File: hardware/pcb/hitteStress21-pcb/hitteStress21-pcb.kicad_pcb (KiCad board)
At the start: 2 copper layers, 90 x 119 mm, 17 parts, among them J1 Conn_01x02_Female, J2 Conn_01x05, J3 Conn_01x03, U1 HTCC-AB01, U2 GPS

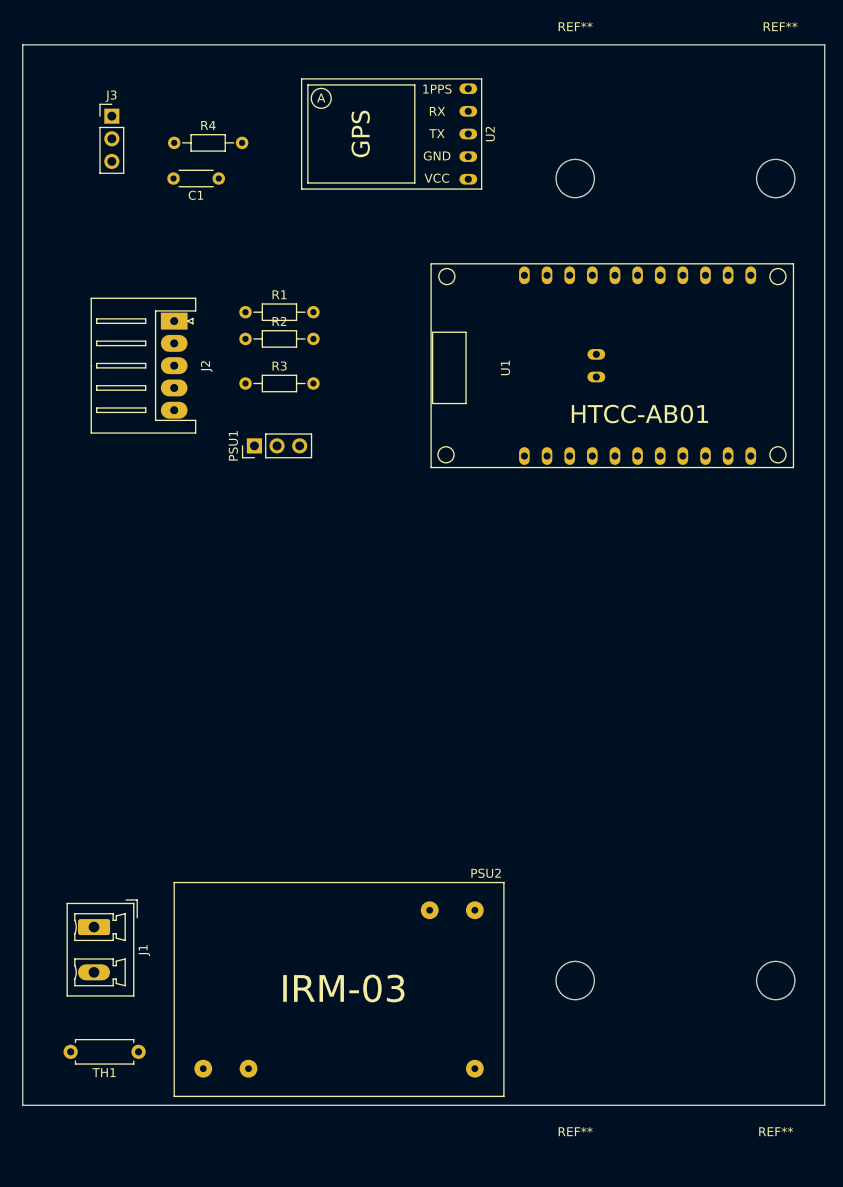
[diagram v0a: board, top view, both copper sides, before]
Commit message: Updates on footprints
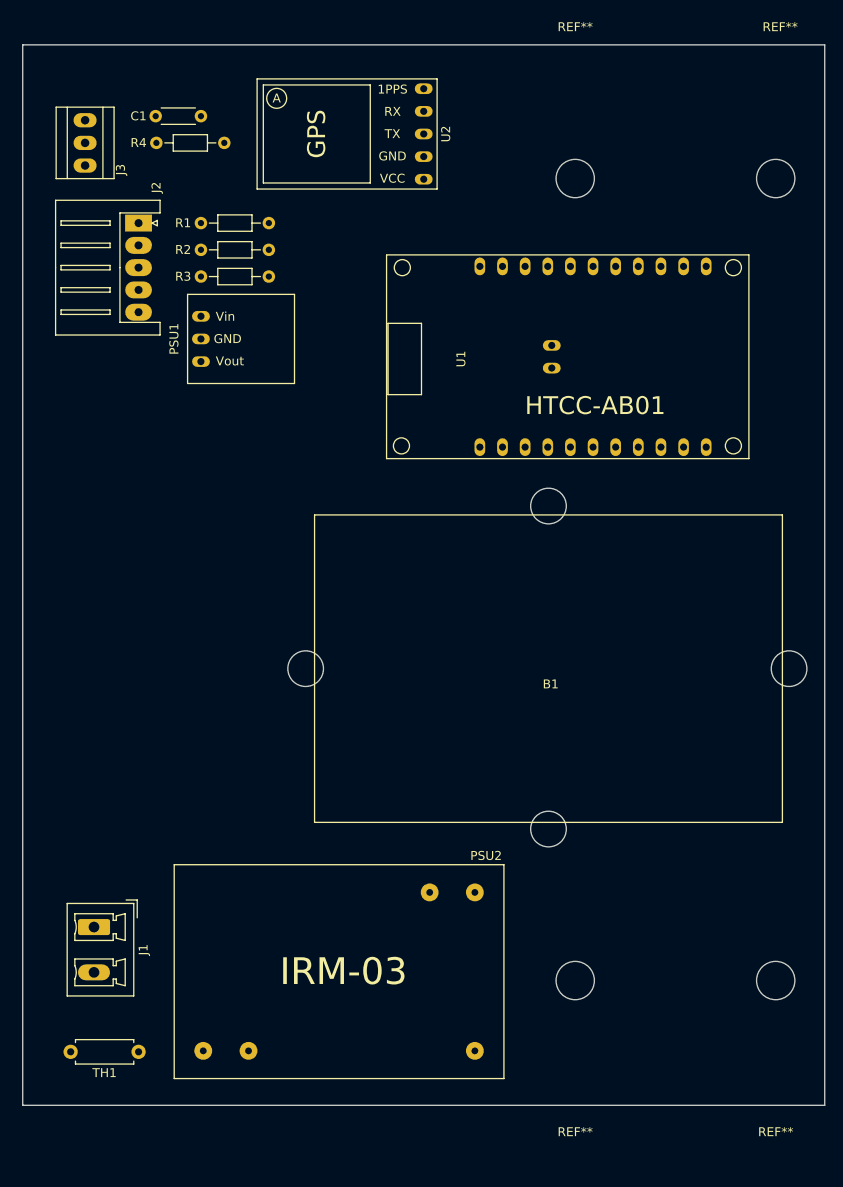
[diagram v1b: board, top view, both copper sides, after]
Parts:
- added B1: LiPo_3V7, hitteStress21-pcb:LiPo_3V7_2000mAh_JST-PH, F.Cu at (220.0, 107.0)
- J3: footprint Connector_PinHeader_2.54mm:PinHeader_1x03_P2.54mm_Vertical -> hitteStress21-pcb:Wurth_2109_p2.54
- PSU1: footprint Connector_PinHeader_2.54mm:PinHeader_1x03_P2.54mm_Vertical -> hitteStress21-pcb:MINIDCBOOST5V
- moved PSU1 13.4 mm to (181.0, 70.0)
- moved R3 13.0 mm to (181.0, 63.0)
- moved J2 11.7 mm to (174.0, 57.0)
- moved R1 11.2 mm to (181.0, 57.0)
- moved R2 11.2 mm to (181.0, 60.0)
- moved C1 7.28 mm to (181.0, 45.0)
- moved U1 5.10 mm to (225.0, 72.0)
- moved U2 5.00 mm to (206.0, 47.0)
- moved J3 4.24 mm to (168.0, 48.0), turned to 90 degrees
- moved PSU2 2.00 mm to (215.0, 129.0)
- moved R4 2.00 mm to (176.0, 48.0)
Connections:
- R1 pad 2: /SDS011_RX -> /SDS011_TX
- R2 pad 2: /SDS011_TX -> /SDS011_RX

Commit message: PCB design updates
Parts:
- added G***: LOGO_LogoRFSee_37x8mm, hitteStress21-pcb:LOGO_LogoRFSee_37x8mm, F.Cu at (219.0, 108.0)
- added G***: LOGO, hitteStress21-pcb:TTN_Apld_Logo_17x17mm_silk, F.Cu at (177.0, 97.0)
- added J4: Conn_01x02, hitteStress21-pcb:Wurth_2109_P2.54_2x1, F.Cu at (167.5, 85.5)
- moved J1 11.5 mm to (169.0, 124.5)
- moved J2 7.52 mm to (173.5, 64.5)
- moved PSU1 7.52 mm to (180.5, 77.5)
- moved R1 7.52 mm to (180.5, 64.5)
- moved R2 7.52 mm to (180.5, 67.5)
- moved R3 7.52 mm to (180.5, 70.5)
- moved U2 5.15 mm to (208.5, 51.5)
- moved C1 4.53 mm to (180.5, 49.5)
- moved J3 4.53 mm to (167.5, 52.5)
- moved R4 4.53 mm to (175.5, 52.5)
- moved PSU2 3.00 mm to (215.0, 126.0)
- moved TH1 3.00 mm to (174.0, 147.0)
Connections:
- R1 pad 2: /SDS011_TX -> /SDS011_TXD
- R2 pad 2: /SDS011_RX -> /SDS011_RXD
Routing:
- net GND: track 0.00 -> 161.1 mm, vias 0 -> 64
- net /3V3: track 0.00 -> 100.4 mm
- net /5V: track 0.00 -> 100.0 mm
- net /PV: track 0.00 -> 76.5 mm
- net /AM2305_DATA: track 0.00 -> 55.0 mm
- net /3V3_EXT: track 0.00 -> 42.4 mm
- net /SDS011_TXD: track 0.00 -> 42.3 mm
- net /GPS_RXD: track 0.00 -> 40.2 mm
- net /GPS_TXD: track 0.00 -> 37.9 mm
- net Net-(J1-Pad1): track 0.00 -> 32.8 mm
- net /SDS011_RXD: track 0.00 -> 32.6 mm
- net Net-(J1-Pad2): track 0.00 -> 18.5 mm
- net /5V_EXT: track 0.00 -> 14.7 mm
- net Net-(J2-Pad4): track 0.00 -> 7.62 mm
- net Net-(PSU2-Pad1): track 0.00 -> 7.31 mm
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- added copper zone on B.Cu, net GND
- added copper zone on F.Cu, net GND
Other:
- board size 90 x 119 mm -> 90 x 109.9 mm
- board text added: "+"
- board text added: "-"
- board text added: "20210117"
- board text added: "3V3"
- board text added: "AC 220V"
- board text added: "AM2305"
- board text added: "DAT"
- board text added: "GND"
- board text added: "Hittestress sensor V2"
- board text added: "PV"
- board text added: "SDS011"
- board text added: "Stichting IoT Apeldoorn e/o www.iot-apeldoorn.ml"

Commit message: Modified HTCC-AB01 footprint and updated PCB accordingly
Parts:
- moved U1 8.06 mm to (217.0, 71.0)
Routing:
- net GND: track 161.1 -> 65.7 mm, vias 64 -> 62
- net /PV: track 76.5 -> 43.1 mm
- net /GPS_TXD: track 37.9 -> 61.3 mm
- net /3V3: track 100.4 -> 77.2 mm
- net /GPS_RXD: track 40.2 -> 61.9 mm
- net /3V3_EXT: track 42.4 -> 59.5 mm
- net /5V: track 100.0 -> 117.0 mm
- net /AM2305_DATA: track 55.0 -> 68.4 mm
- net /SDS011_RXD: track 32.6 -> 40.4 mm
- net /SDS011_TXD: track 42.3 -> 36.7 mm
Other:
- board text added: "20210216"
- board text removed: "20210117"

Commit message: UPdate PCD, added support holes for antenna supports
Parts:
- moved U2 4.00 mm to (212.5, 51.5)
- moved G*** 3.50 mm to (173.5, 97.0)
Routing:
- net /GPS_TXD: track 61.3 -> 57.3 mm
- net /GPS_RXD: track 61.9 -> 57.9 mm
- net /3V3_EXT: track 59.5 -> 55.5 mm
- net /AM2305_DATA: track 68.4 -> 71.3 mm
- net GND: vias 62 -> 61
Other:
- outline, holes or cut-outs redrawn
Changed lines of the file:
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@@
   (general
     (thickness 1.6)
-    (drawings 16)
-    (tracks 160)
+    (drawings 22)
+    (tracks 158)
     (zones 0)
     (modules 21)
@@
   )
   (setup
-    (last_trace_width 1)
+    (last_trace_width 0.25)
     (user_trace_width 0.5)
     (user_trace_width 0.75)
@@
   )
   (module hitteStress21-pcb:GPS (layer F.Cu)
-    (at 208.5 51.5)
+    (at 212.5 51.5)
     (fp_text reference U2 (at 2.75 5.5 180) (layer F.SilkS)
       (effects (font (size 1 1) (thickness 0.15)))
@@
   )
   (module hitteStress21-pcb:TTN_Apld_Logo_17x17mm_silk (layer F.Cu)
-    (at 177 97)
+    (at 173.5 97)
     (fp_text reference G*** (at 0 0) (layer F.SilkS) hide
       (effects (font (size 1.524 1.524) (thickness 0.3)))
@@
       (net 13 "Net-(U1-Pad22)"))
   )
-  (gr_text "Hittestress\nsensor V2" (at 177 110.5) (layer F.SilkS)
+  (gr_circle (center 185 110) (end 187.25 110) (layer Edge.Cuts) (width 0.1))
+  (gr_circle (center 185 102.38) (end 186.75 102.38) (layer Edge.Cuts) (width 0.1))
+  (gr_circle (center 243.5 73.5) (end 245.75 73.5) (layer Edge.Cuts) (width 0.1))
+  (gr_circle (center 243.5 65.88) (end 245.25 65.88) (layer Edge.Cuts) (width 0.1))
+  (gr_circle (center 188.5 49.38) (end 190.25 49.38) (layer Edge.Cuts) (width 0.1))
+  (gr_circle (center 188.5 57) (end 190.75 57) (layer Edge.Cuts) (width 0.1))
+  (gr_text "Hittestress\nsensor V2" (at 173.5 110.5) (layer F.SilkS)
     (effects (font (size 2 2) (thickness 0.5)))
   )
-  (gr_text "Stichting IoT Apeldoorn e/o\nwww.iot-apeldoorn.ml" (at 177 117.5) (layer F.SilkS)
+  (gr_text "Stichting IoT Apeldoorn e/o\nwww.iot-apeldoorn.ml" (at 173.5 117.5) (layer F.SilkS)
     (effects (font (size 1 1) (thickness 0.25)))
   )
@@
   (via (at 165 110) (size 0.8) (drill 0.4) (layers F.Cu B.Cu) (net 2))
   (via (at 175 110) (size 0.8) (drill 0.4) (layers F.Cu B.Cu) (net 2))
-  (via (at 185 110) (size 0.8) (drill 0.4) (layers F.Cu B.Cu) (net 2))
   (via (at 205 110) (size 0.8) (drill 0.4) (layers F.Cu B.Cu) (net 2))
   (via (at 205 120) (size 0.8) (drill 0.4) (layers F.Cu B.Cu) (net 2))
@@
   (via (at 205 100) (size 0.8) (drill 0.4) (layers F.Cu B.Cu) (net 2))
   (via (at 195 100) (size 0.8) (drill 0.4) (layers F.Cu B.Cu) (net 2))
-  (via (at 185 100) (size 0.8) (drill 0.4) (layers F.Cu B.Cu) (net 2))
   (via (at 175 100) (size 0.8) (drill 0.4) (layers F.Cu B.Cu) (net 2))
   (via (at 165 100) (size 0.8) (drill 0.4) (layers F.Cu B.Cu) (net 2))
@@
   (via (at 194.5 49.5) (size 0.8) (drill 0.4) (layers F.Cu B.Cu) (net 2))
   (via (at 204.5 49.5) (size 0.8) (drill 0.4) (layers F.Cu B.Cu) (net 2))
-  (via (at 215 50) (size 0.8) (drill 0.4) (layers F.Cu B.Cu) (net 2))
   (via (at 235 50) (size 0.8) (drill 0.4) (layers F.Cu B.Cu) (net 2))
+  (via (at 235 80) (size 0.8) (drill 0.4) (layers F.Cu B.Cu) (net 2))
+  (via (at 235 60) (size 0.8) (drill 0.4) (layers F.Cu B.Cu) (net 2))
   (segment (start 186.34 139.84) (end 186.34 146.89) (width 1.5) (layer F.Cu) (net 3))
   (segment (start 169 124.5) (end 174.5 124.5) (width 1.5) (layer F.Cu) (net 3))
@@
   (segment (start 176.5 72) (end 178 70.5) (width 0.5) (layer B.Cu) (net 7))
   (segment (start 167.5 52.5) (end 175.5 52.5) (width 0.5) (layer F.Cu) (net 9))
+  (segment (start 226.5 58.5) (end 227.16 59.16) (width 0.5) (layer F.Cu) (net 9))
   (segment (start 227.16 59.16) (end 227.16 60.86) (width 0.5) (layer F.Cu) (net 9))
-  (segment (start 226.5 58.5) (end 227.16 59.16) (width 0.5) (layer F.Cu) (net 9))
+  (segment (start 178 50) (end 178 49) (width 0.5) (layer F.Cu) (net 9))
+  (segment (start 182.5 44.5) (end 194.035082 44.5) (width 0.5) (layer F.Cu) (net 9))
+  (segment (start 175.5 52.5) (end 178 50) (width 0.5) (layer F.Cu) (net 9))
+  (segment (start 178 49) (end 182.5 44.5) (width 0.5) (layer F.Cu) (net 9))
   (segment (start 208.035082 58.5) (end 226.5 58.5) (width 0.5) (layer F.Cu) (net 9))
-  (segment (start 178 50) (end 178 49) (width 0.5) (layer F.Cu) (net 9))
-  (segment (start 175.5 52.5) (end 178 50) (width 0.5) (layer F.Cu) (net 9))
-  (segment (start 178 49) (end 179 48) (width 0.5) (layer F.Cu) (net 9))
-  (segment (start 179 48) (end 197.535082 48) (width 0.5) (layer F.Cu) (net 9))
-  (segment (start 197.535082 48) (end 208.035082 58.5) (width 0.5) (layer F.Cu) (net 9))
+  (segment (start 194.035082 44.5) (end 208.035082 58.5) (width 0.5) (layer F.Cu) (net 9))
   (segment (start 188.12 75.88) (end 188.12 70.5) (width 1) (layer F.Cu) (net 10))
   (segment (start 180.5 80.04) (end 183.96 80.04) (width 1) (layer F.Cu) (net 10))
@@
   (segment (start 226.6 45.3) (end 233.4 52.1) (width 0.5) (layer F.Cu) (net 17))
   (segment (start 219.9 45.3) (end 226.6 45.3) (width 0.5) (layer F.Cu) (net 17))
-  (segment (start 208.5 48.96) (end 216.24 48.96) (width 0.5) (layer F.Cu) (net 17))
   (segment (start 233.4 52.1) (end 233.4 69.8) (width 0.5) (layer F.Cu) (net 17))
+  (segment (start 216.24 48.96) (end 212.5 48.96) (width 0.5) (layer F.Cu) (net 17))
   (segment (start 188.12 64.5) (end 220.5 64.5) (width 0.5) (layer F.Cu) (net 18))
   (segment (start 222.08 62.92) (end 222.08 60.86) (width 0.5) (layer F.Cu) (net 18))
@@
   (segment (start 232.4 69.32) (end 222.08 79.64) (width 0.5) (layer F.Cu) (net 19))
   (segment (start 215.1 51.5) (end 220.2 46.4) (width 0.5) (layer F.Cu) (net 19))
-  (segment (start 208.5 51.5) (end 215.1 51.5) (width 0.5) (layer F.Cu) (net 19))
   (segment (start 226.1 46.4) (end 232.4 52.7) (width 0.5) (layer F.Cu) (net 19))
   (segment (start 220.2 46.4) (end 226.1 46.4) (width 0.5) (layer F.Cu) (net 19))
   (segment (start 232.4 52.7) (end 232.4 69.32) (width 0.5) (layer F.Cu) (net 19))
-  (segment (start 216.1 75) (end 211.92 79.18) (width 0.5) (layer F.Cu) (net 26))
-  (segment (start 231.4 58.9) (end 231.4 68.8) (width 0.5) (layer F.Cu) (net 26))
-  (segment (start 211.92 79.18) (end 211.92 81.14) (width 0.5) (layer F.Cu) (net 26))
-  (segment (start 231.4 68.8) (end 225.2 75) (width 0.5) (layer F.Cu) (net 26))
-  (segment (start 208.52 56.6) (end 210.6 56.6) (width 0.5) (layer F.Cu) (net 26))
-  (segment (start 208.5 56.58) (end 208.52 56.6) (width 0.5) (layer F.Cu) (net 26))
-  (segment (start 210.6 56.6) (end 211.5 57.5) (width 0.5) (layer F.Cu) (net 26))
-  (segment (start 230 57.5) (end 231.4 58.9) (width 0.5) (layer F.Cu) (net 26))
-  (segment (start 225.2 75) (end 216.1 75) (width 0.5) (layer F.Cu) (net 26))
-  (segment (start 211.5 57.5) (end 230 57.5) (width 0.5) (layer F.Cu) (net 26))
+  (segment (start 212.5 51.5) (end 215.1 51.5) (width 0.5) (layer F.Cu) (net 19))
+  (segment (start 216.58 56.58) (end 212.5 56.58) (width 0.5) (layer F.Cu) (net 26))
+  (segment (start 217.5 57.5) (end 216.58 56.58) (width 0.5) (layer F.Cu) (net 26))
+  (segment (start 231.4 58.9) (end 230 57.5) (width 0.5) (layer F.Cu) (net 26))
+  (segment (start 211.92 81.14) (end 211.92 79.18) (width 0.5) (layer F.Cu) (net 26))
+  (segment (start 230 57.5) (end 217.5 57.5) (width 0.5) (layer F.Cu) (net 26))
+  (segment (start 225.2 75) (end 231.4 68.8) (width 0.5) (layer F.Cu) (net 26))
+  (segment (start 211.92 79.18) (end 216.1 75) (width 0.5) (layer F.Cu) (net 26))
+  (segment (start 216.1 75) (end 225.2 75) (width 0.5) (layer F.Cu) (net 26))
+  (segment (start 231.4 68.8) (end 231.4 58.9) (width 0.5) (layer F.Cu) (net 26))
   (segment (start 167.5 86.77) (end 203.73 86.77) (width 1) (layer F.Cu) (net 28))
   (segment (start 206.84 83.66) (end 206.84 81.14) (width 1) (layer F.Cu) (net 28))

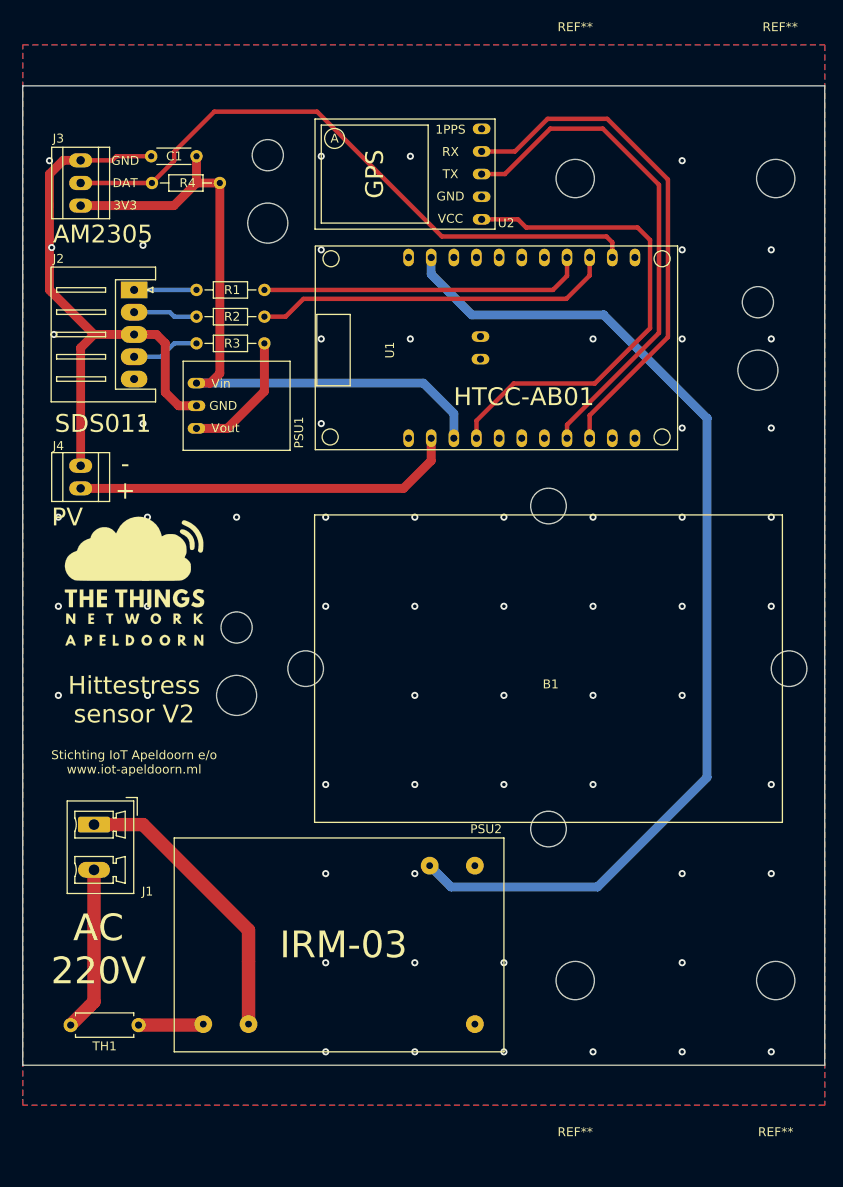
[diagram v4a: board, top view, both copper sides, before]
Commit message: Start redesign PCB
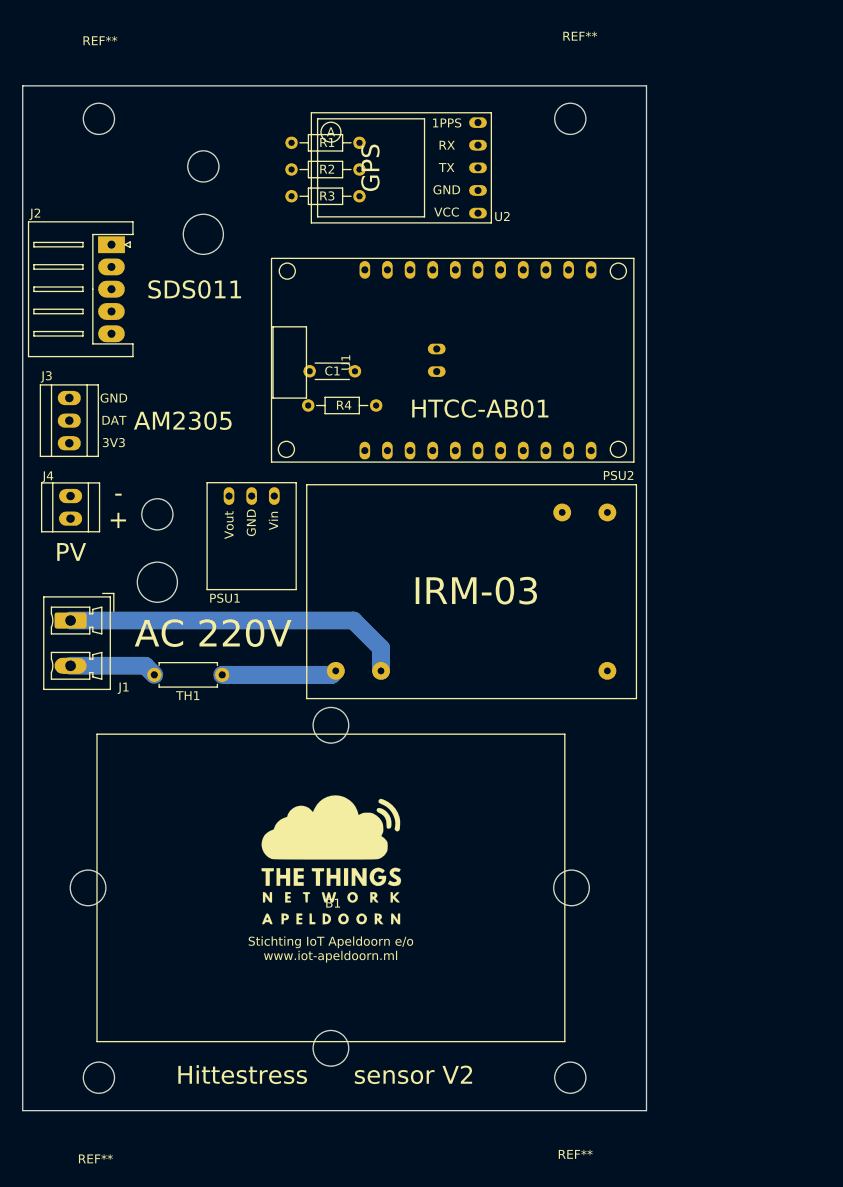
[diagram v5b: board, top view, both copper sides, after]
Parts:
- removed the REF** at (245.5, 142.0)
- removed the REF** at (245.5, 52.0)
- removed the REF** at (223.0, 142.0)
- removed the REF** at (223.0, 52.0)
- added REF**: MountingHole_3.5mm, MountingHole:MountingHole_3.5mm, F.Cu at (169.6, 152.9)
- added REF**: MountingHole_3.5mm, MountingHole:MountingHole_3.5mm, F.Cu at (169.6, 45.3)
- added REF**: MountingHole_3.5mm, MountingHole:MountingHole_3.5mm, F.Cu at (222.4, 45.3)
- added REF**: MountingHole_3.5mm, MountingHole:MountingHole_3.5mm, F.Cu at (222.4, 152.9)
- moved PSU2 42.3 mm to (229.9, 86.4)
- moved TH1 40.4 mm to (183.4, 107.7)
- moved G*** 38.3 mm to (195.6, 128.3)
- moved G*** 36.2 mm to (194.5, 134.6)
- moved B1 34.7 mm to (195.6, 131.6)
- moved R4 30.5 mm to (193.0, 77.5)
- moved C1 30.0 mm to (198.3, 73.6)
- moved J3 26.7 mm to (166.2, 79.2)
- moved J1 23.1 mm to (166.4, 101.6)
- moved R1 19.7 mm to (191.2, 48.0)
- moved R2 19.7 mm to (191.2, 51.0)
- moved R3 19.7 mm to (191.2, 54.0)
- moved PSU1 11.9 mm to (186.7, 87.6), turned to 0 degrees
- moved J2 5.68 mm to (171.0, 59.4)
- moved U1 5.10 mm to (212.1, 72.4)
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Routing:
- net /5V: track 117.0 -> 0.00 mm
- net /3V3: track 77.2 -> 0.00 mm
- net /AM2305_DATA: track 71.3 -> 0.00 mm
- net GND: track 65.7 -> 0.00 mm, vias 61 -> 0
- net /GPS_RXD: track 57.9 -> 0.00 mm
- net /GPS_TXD: track 57.3 -> 0.00 mm
- net /3V3_EXT: track 55.5 -> 0.00 mm
- net /PV: track 43.1 -> 0.00 mm
- net /SDS011_RXD: track 40.4 -> 0.00 mm
- net /SDS011_TXD: track 36.7 -> 0.00 mm
- net /5V_EXT: track 14.7 -> 0.00 mm
- net Net-(J1-Pad2): track 18.5 -> 9.82 mm
- net Net-(J2-Pad4): track 7.62 -> 0.00 mm
- net /PM_TX: track 7.21 -> 0.00 mm
- net /PM_RX: track 7.00 -> 0.00 mm
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- removed copper zone on B.Cu, net GND
- removed copper zone on F.Cu, net GND
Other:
- board size 90 x 109.9 mm -> 70 x 115 mm
- board text added: "20210406"
- board text added: "Hittestress"
- board text added: "sensor V2"
- board text removed: "20210216"
- board text removed: "Hittestress sensor V2"
